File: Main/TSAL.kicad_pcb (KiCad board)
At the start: 2 copper layers, 140 x 70 mm, 156 parts, among them J1 Micro-Fit, J2 Mini-SPOX, J3 Mini-SPOX, J4 Mini-SPOX, J5 Mini-SPOX, Q1 IRLML2502, Q10 NPN, Q11 MJD122, Q12 PNP, Q2 IRLML2502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

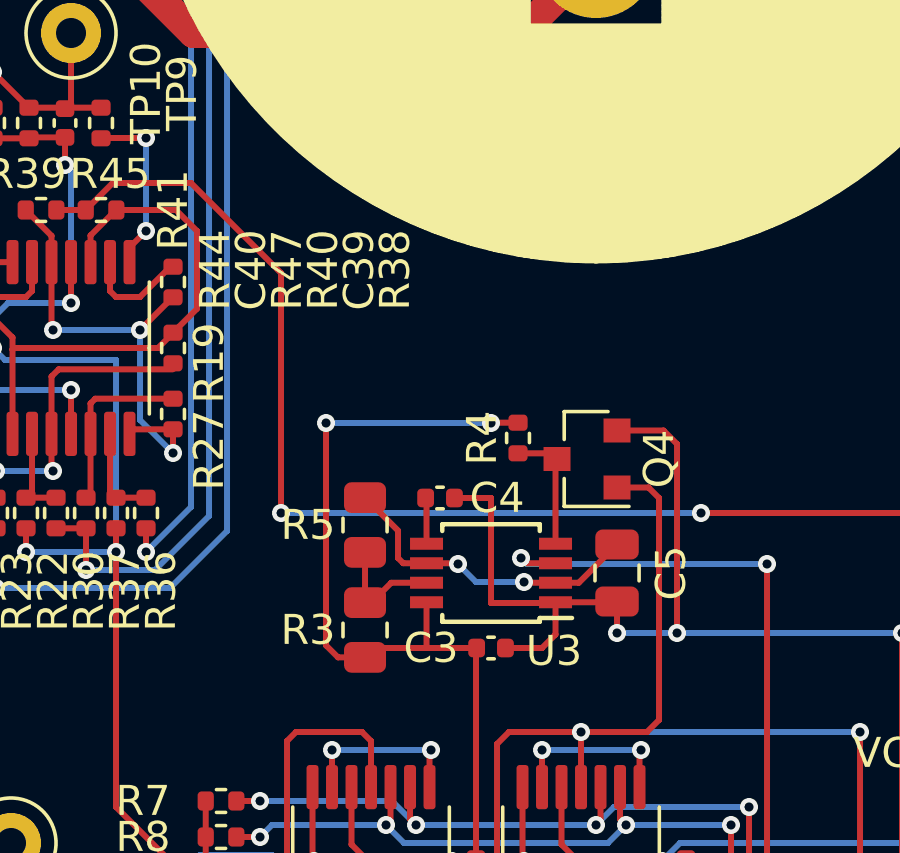
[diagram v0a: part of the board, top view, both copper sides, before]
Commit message: Fixed LMC555 footprint error on main TSAL board
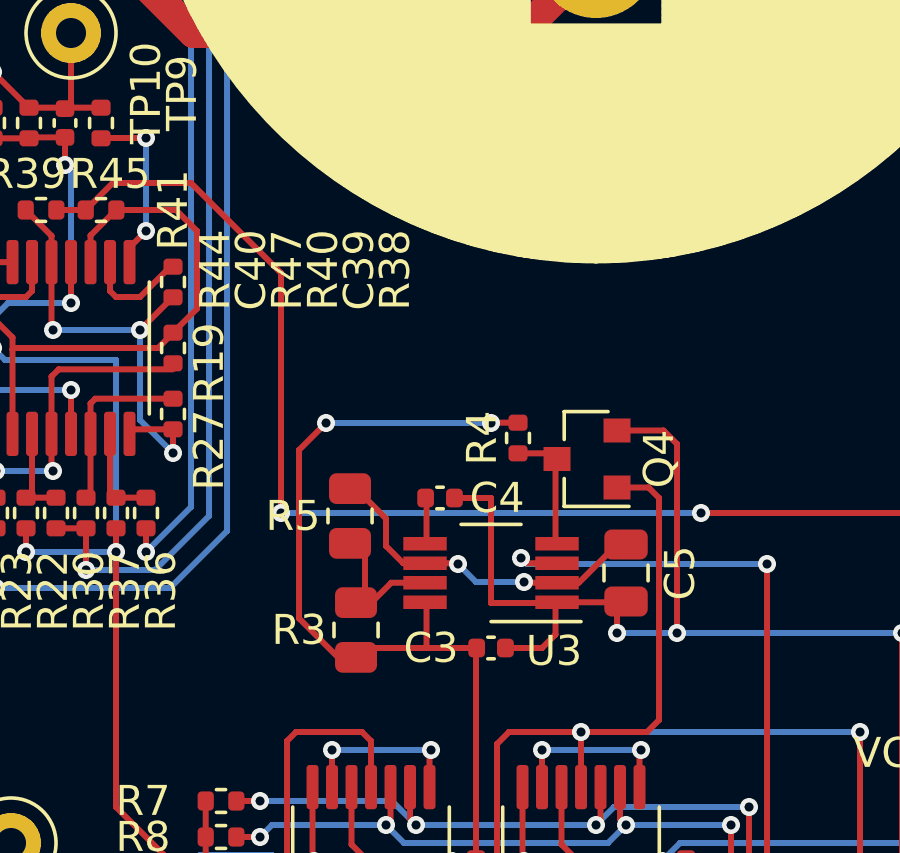
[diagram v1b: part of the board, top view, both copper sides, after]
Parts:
- U3: footprint archive:TSSOP-8_3x3mm_P0.65mm -> Package_SO:VSSOP-8_3.0x3.0mm_P0.65mm
- moved R5 0.58 mm to (85.3, 109.1)
- moved C5 0.30 mm to (94.5, 111.0)
- moved R3 0.30 mm to (85.5, 112.9)
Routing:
- net VCC: track 138.7 -> 139.4 mm
